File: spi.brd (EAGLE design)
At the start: 34 x 33 mm, 5 parts, among them IC2 25AA080SN, IC3 25AA080P, X1 2510-

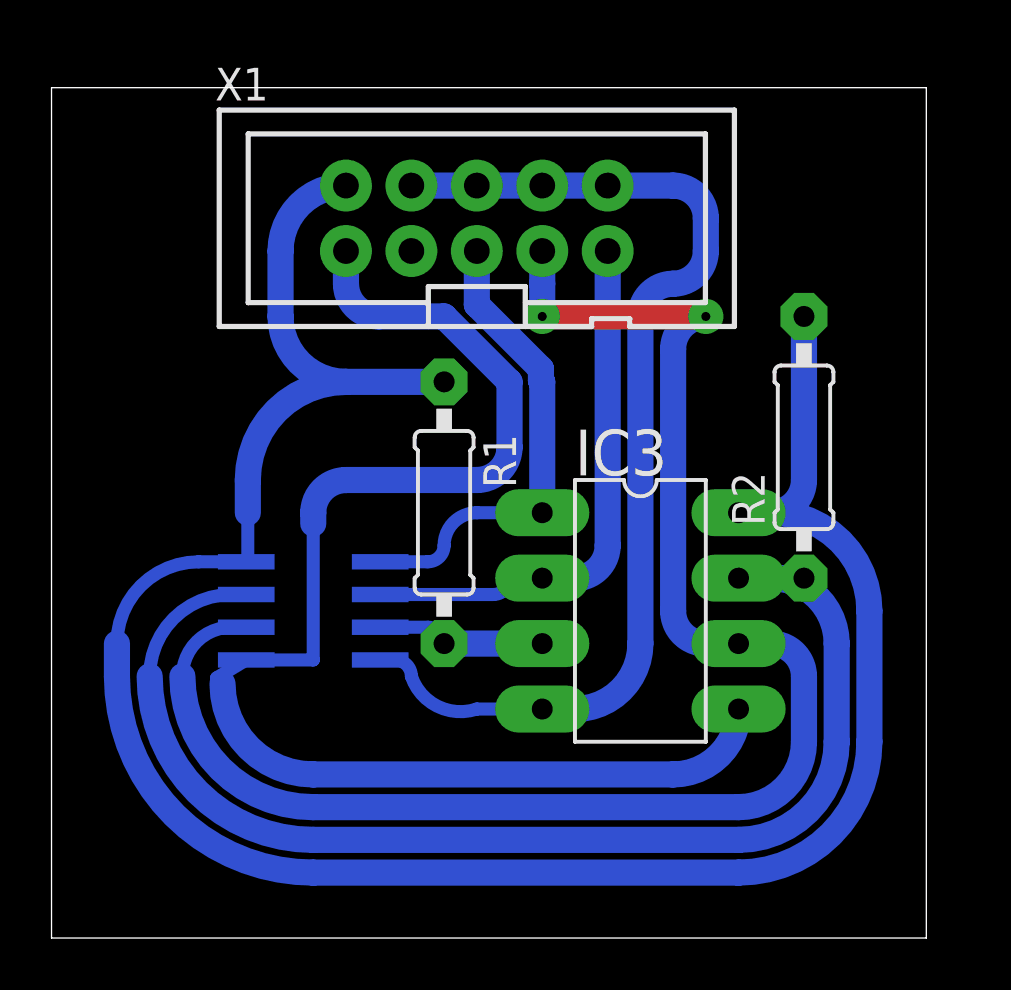
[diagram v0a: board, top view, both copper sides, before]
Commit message: Added ground polygon
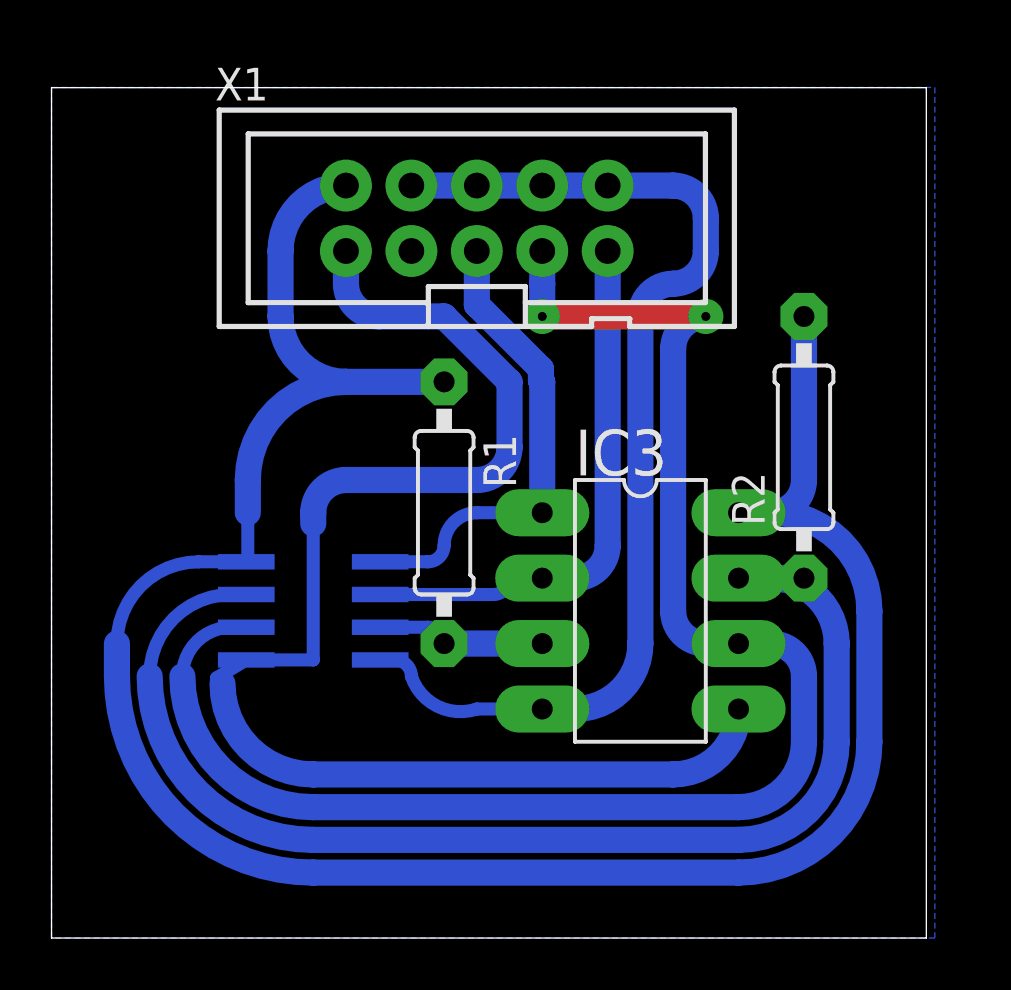
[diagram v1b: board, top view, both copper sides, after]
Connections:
- net N$1 renamed GND
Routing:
- added copper zone on layer 16, net GND
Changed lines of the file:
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@@
 <grid distance="50" unitdist="mil" unit="mm" style="lines" multiple="1" display="yes" altdistance="5" altunitdist="mil" altunit="mm"/>
 <layers>
-<layer number="1" name="Top" color="4" fill="1" visible="yes" active="yes"/>
+<layer number="1" name="Top" color="4" fill="1" visible="no" active="yes"/>
 <layer number="16" name="Bottom" color="1" fill="1" visible="yes" active="yes"/>
 <layer number="17" name="Pads" color="2" fill="1" visible="yes" active="yes"/>
 <layer number="18" name="Vias" color="2" fill="1" visible="yes" active="yes"/>
-<layer number="19" name="Unrouted" color="6" fill="1" visible="yes" active="yes"/>
+<layer number="19" name="Unrouted" color="6" fill="1" visible="no" active="yes"/>
 <layer number="20" name="Dimension" color="24" fill="1" visible="yes" active="yes"/>
-<layer number="21" name="tPlace" color="7" fill="1" visible="yes" active="yes"/>
-<layer number="22" name="bPlace" color="7" fill="1" visible="yes" active="yes"/>
-<layer number="23" name="tOrigins" color="15" fill="1" visible="yes" active="yes"/>
-<layer number="24" name="bOrigins" color="15" fill="1" visible="yes" active="yes"/>
-<layer number="25" name="tNames" color="7" fill="1" visible="yes" active="yes"/>
-<layer number="26" name="bNames" color="7" fill="1" visible="yes" active="yes"/>
-<layer number="27" name="tValues" color="7" fill="1" visible="yes" active="yes"/>
-<layer number="28" name="bValues" color="7" fill="1" visible="yes" active="yes"/>
-<layer number="29" name="tStop" color="7" fill="3" visible="yes" active="yes"/>
-<layer number="30" name="bStop" color="7" fill="6" visible="yes" active="yes"/>
-<layer number="31" name="tCream" color="7" fill="4" visible="yes" active="yes"/>
-<layer number="32" name="bCream" color="7" fill="5" visible="yes" active="yes"/>
-<layer number="33" name="tFinish" color="6" fill="3" visible="yes" active="yes"/>
-<layer number="34" name="bFinish" color="6" fill="6" visible="yes" active="yes"/>
-<layer number="35" name="tGlue" color="7" fill="4" visible="yes" active="yes"/>
-<layer number="36" name="bGlue" color="7" fill="5" visible="yes" active="yes"/>
-<layer number="37" name="tTest" color="7" fill="1" visible="yes" active="yes"/>
-<layer number="38" name="bTest" color="7" fill="1" visible="yes" active="yes"/>
-<layer number="39" name="tKeepout" color="4" fill="11" visible="yes" active="yes"/>
-<layer number="40" name="bKeepout" color="1" fill="11" visible="yes" active="yes"/>
-<layer number="41" name="tRestrict" color="4" fill="10" visible="yes" active="yes"/>
+<layer number="21" name="tPlace" color="7" fill="1" visible="no" active="yes"/>
+<layer number="22" name="bPlace" color="7" fill="1" visible="no" active="yes"/>
+<layer number="23" name="tOrigins" color="15" fill="1" visible="no" active="yes"/>
+<layer number="24" name="bOrigins" color="15" fill="1" visible="no" active="yes"/>
+<layer number="25" name="tNames" color="7" fill="1" visible="no" active="yes"/>
+<layer number="26" name="bNames" color="7" fill="1" visible="no" active="yes"/>
+<layer number="27" name="tValues" color="7" fill="1" visible="no" active="yes"/>
+<layer number="28" name="bValues" color="7" fill="1" visible="no" active="yes"/>
+<layer number="29" name="tStop" color="7" fill="3" visible="no" active="yes"/>
+<layer number="30" name="bStop" color="7" fill="6" visible="no" active="yes"/>
+<layer number="31" name="tCream" color="7" fill="4" visible="no" active="yes"/>
+<layer number="32" name="bCream" color="7" fill="5" visible="no" active="yes"/>
+<layer number="33" name="tFinish" color="6" fill="3" visible="no" active="yes"/>
+<layer number="34" name="bFinish" color="6" fill="6" visible="no" active="yes"/>
+<layer number="35" name="tGlue" color="7" fill="4" visible="no" active="yes"/>
+<layer number="36" name="bGlue" color="7" fill="5" visible="no" active="yes"/>
+<layer number="37" name="tTest" color="7" fill="1" visible="no" active="yes"/>
+<layer number="38" name="bTest" color="7" fill="1" visible="no" active="yes"/>
+<layer number="39" name="tKeepout" color="4" fill="11" visible="no" active="yes"/>
+<layer number="40" name="bKeepout" color="1" fill="11" visible="no" active="yes"/>
+<layer number="41" name="tRestrict" color="4" fill="10" visible="no" active="yes"/>
 <layer number="42" name="bRestrict" color="1" fill="10" visible="yes" active="yes"/>
-<layer number="43" name="vRestrict" color="2" fill="10" visible="yes" active="yes"/>
-<layer number="44" name="Drills" color="7" fill="1" visible="yes" active="yes"/>
-<layer number="45" name="Holes" color="7" fill="1" visible="yes" active="yes"/>
-<layer number="46" name="Milling" color="3" fill="1" visible="yes" active="yes"/>
-<layer number="47" name="Measures" color="7" fill="1" visible="yes" active="yes"/>
-<layer number="48" name="Document" color="7" fill="1" visible="yes" active="yes"/>
-<layer number="49" name="Reference" color="7" fill="1" visible="yes" active="yes"/>
-<layer number="51" name="tDocu" color="7" fill="1" visible="yes" active="yes"/>
-<layer number="52" name="bDocu" color="7" fill="1" visible="yes" active="yes"/>
+<layer number="43" name="vRestrict" color="2" fill="10" visible="no" active="yes"/>
+<layer number="44" name="Drills" color="7" fill="1" visible="no" active="yes"/>
+<layer number="45" name="Holes" color="7" fill="1" visible="no" active="yes"/>
+<layer number="46" name="Milling" color="3" fill="1" visible="no" active="yes"/>
+<layer number="47" name="Measures" color="7" fill="1" visible="no" active="yes"/>
+<layer number="48" name="Document" color="7" fill="1" visible="no" active="yes"/>
+<layer number="49" name="Reference" color="7" fill="1" visible="no" active="yes"/>
+<layer number="51" name="tDocu" color="7" fill="1" visible="no" active="yes"/>
+<layer number="52" name="bDocu" color="7" fill="1" visible="no" active="yes"/>
 <layer number="88" name="SimResults" color="9" fill="1" visible="no" active="no"/>
 <layer number="89" name="SimProbes" color="9" fill="1" visible="no" active="no"/>
@@
 <wire x1="42.85" y1="49.52" x2="8.89" y2="49.52" width="0" layer="20"/>
 <wire x1="8.89" y1="49.52" x2="8.89" y2="16.51" width="0" layer="20"/>
+<polygon width="0.3048" layer="42">
+<vertex x="19.05" y="27.94"/>
+<vertex x="19.05" y="34.29"/>
+<vertex x="25.4" y="34.29"/>
+<vertex x="25.4" y="27.94"/>
+</polygon>
 </plain>
 <attributes>
@@
 </elements>
 <signals>
-<signal name="N$1">
-<contactref element="IC2" pad="4"/>
-<contactref element="IC3" pad="4"/>
-<contactref element="X1" pad="4"/>
-<contactref element="X1" pad="6"/>
-<contactref element="X1" pad="8"/>
-<contactref element="X1" pad="10"/>
-<wire x1="21.65" y1="27.305" x2="22.225" y2="27.305" width="0.508" layer="16"/>
-<wire x1="22.225" y1="27.305" x2="22.86" y2="26.67" width="0.508" layer="16" curve="-90"/>
-<wire x1="22.86" y1="26.67" x2="25.4" y2="25.4" width="0.508" layer="16" curve="90"/>
-<wire x1="25.4" y1="25.4" x2="27.94" y2="25.4" width="0.508" layer="16"/>
-<wire x1="27.94" y1="25.4" x2="29.21" y2="25.4" width="1.016" layer="16"/>
-<wire x1="29.21" y1="25.4" x2="31.75" y2="27.94" width="1.016" layer="16" curve="90"/>
-<wire x1="31.75" y1="27.94" x2="31.75" y2="40.64" width="1.016" layer="16"/>
-<wire x1="31.75" y1="40.64" x2="33.02" y2="41.91" width="1.016" layer="16" curve="-90"/>
-<wire x1="33.02" y1="41.91" x2="34.29" y2="43.18" width="1.016" layer="16" curve="90"/>
-<wire x1="34.29" y1="43.18" x2="34.29" y2="44.45" width="1.016" layer="16"/>
-<wire x1="34.29" y1="44.45" x2="33.02" y2="45.72" width="1.016" layer="16" curve="90"/>
-<wire x1="33.02" y1="45.72" x2="30.48" y2="45.72" width="1.016" layer="16"/>
-<wire x1="22.86" y1="45.72" x2="25.4" y2="45.72" width="1.016" layer="16"/>
-<wire x1="25.4" y1="45.72" x2="27.94" y2="45.72" width="1.016" layer="16"/>
-<wire x1="27.94" y1="45.72" x2="30.48" y2="45.72" width="1.016" layer="16"/>
-</signal>
 <signal name="N$2">
 <contactref element="IC2" pad="8"/>
@@
 <wire x1="27.94" y1="27.94" x2="24.13" y2="27.94" width="1.016" layer="16"/>
 </signal>
+<signal name="GND">
+<contactref element="IC2" pad="4"/>
+<contactref element="IC3" pad="4"/>
+<contactref element="X1" pad="4"/>
+<contactref element="X1" pad="6"/>
+<contactref element="X1" pad="8"/>
+<contactref element="X1" pad="10"/>
+<wire x1="21.65" y1="27.305" x2="22.225" y2="27.305" width="0.508" layer="16"/>
+<wire x1="22.225" y1="27.305" x2="22.86" y2="26.67" width="0.508" layer="16" curve="-90"/>
+<wire x1="22.86" y1="26.67" x2="25.4" y2="25.4" width="0.508" layer="16" curve="90"/>
+<wire x1="25.4" y1="25.4" x2="27.94" y2="25.4" width="0.508" layer="16"/>
+<wire x1="27.94" y1="25.4" x2="29.21" y2="25.4" width="1.016" layer="16"/>
+<wire x1="29.21" y1="25.4" x2="31.75" y2="27.94" width="1.016" layer="16" curve="90"/>
+<wire x1="31.75" y1="27.94" x2="31.75" y2="40.64" width="1.016" layer="16"/>
+<wire x1="31.75" y1="40.64" x2="33.02" y2="41.91" width="1.016" layer="16" curve="-90"/>
+<wire x1="33.02" y1="41.91" x2="34.29" y2="43.18" width="1.016" layer="16" curve="90"/>
+<wire x1="34.29" y1="43.18" x2="34.29" y2="44.45" width="1.016" layer="16"/>
+<wire x1="34.29" y1="44.45" x2="33.02" y2="45.72" width="1.016" layer="16" curve="90"/>
+<wire x1="33.02" y1="45.72" x2="30.48" y2="45.72" width="1.016" layer="16"/>
+<wire x1="22.86" y1="45.72" x2="25.4" y2="45.72" width="1.016" layer="16"/>
+<wire x1="25.4" y1="45.72" x2="27.94" y2="45.72" width="1.016" layer="16"/>
+<wire x1="27.94" y1="45.72" x2="30.48" y2="45.72" width="1.016" layer="16"/>
+<polygon width="0.3048" layer="16" isolate="0.3048">
+<vertex x="8.89" y="49.53"/>
+<vertex x="43.18" y="49.53"/>
+<vertex x="43.18" y="16.51"/>
+<vertex x="8.89" y="16.51"/>
+</polygon>
+</signal>
 </signals>

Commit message: Renamed net
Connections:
- net N$2 renamed VCC
- net N$3 renamed SO
- net N$4 renamed HOLD
- net N$5 renamed SCK
- net N$6 renamed SI
- net N$7 renamed CS
- net N$8 renamed WP
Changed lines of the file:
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@@
 </elements>
 <signals>
-<signal name="N$2">
+<signal name="VCC">
 <contactref element="IC2" pad="8"/>
 <contactref element="IC3" pad="8"/>
@@
 <wire x1="16.51" y1="34.29" x2="16.51" y2="33.02" width="1.016" layer="16"/>
 </signal>
-<signal name="N$3">
+<signal name="SO">
 <contactref element="IC2" pad="2"/>
 <contactref element="IC3" pad="2"/>
@@
 <wire x1="30.48" y1="31.75" x2="30.48" y2="43.18" width="1.016" layer="16"/>
 </signal>
-<signal name="N$4">
+<signal name="HOLD">
 <contactref element="IC2" pad="7"/>
 <contactref element="IC3" pad="7"/>
@@
 <wire x1="35.56" y1="30.48" x2="38.1" y2="30.48" width="1.016" layer="16"/>
 </signal>
-<signal name="N$5">
+<signal name="SCK">
 <contactref element="IC2" pad="6"/>
 <contactref element="IC3" pad="6"/>
@@
 <wire x1="27.94" y1="40.64" x2="27.94" y2="41.90991875" width="1.016" layer="16"/>
 </signal>
-<signal name="N$6">
+<signal name="SI">
 <contactref element="IC2" pad="5"/>
 <contactref element="IC3" pad="5"/>
@@
 <wire x1="24.13" y1="40.64" x2="26.67" y2="38.1" width="1.016" layer="16"/>
 </signal>
-<signal name="N$7">
+<signal name="CS">
 <contactref element="IC2" pad="1"/>
 <contactref element="IC3" pad="1"/>
@@
 <wire x1="25.4" y1="41.0942125" x2="25.4" y2="43.18" width="1.016" layer="16"/>
 </signal>
-<signal name="N$8">
+<signal name="WP">
 <contactref element="IC2" pad="3"/>
 <contactref element="R1" pad="2"/>

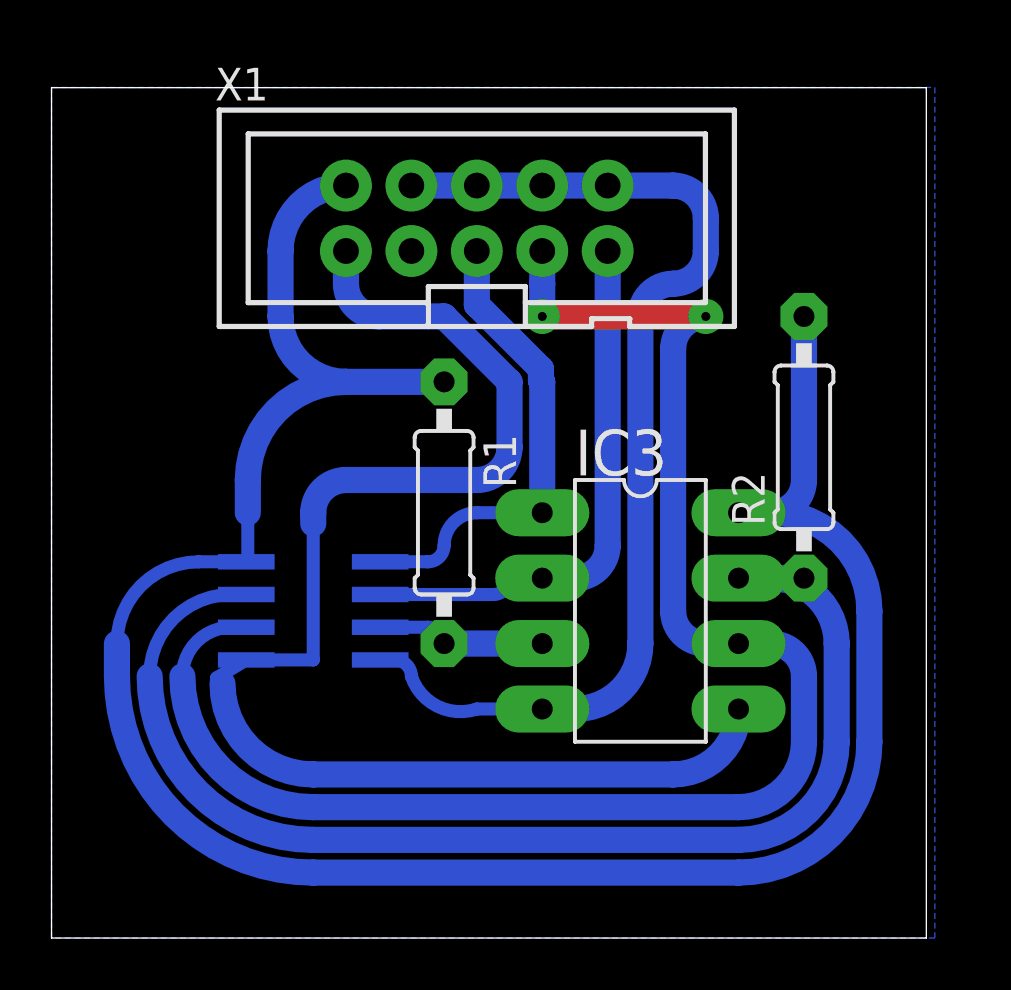
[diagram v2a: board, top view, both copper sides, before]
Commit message: Fixed DRC bugs
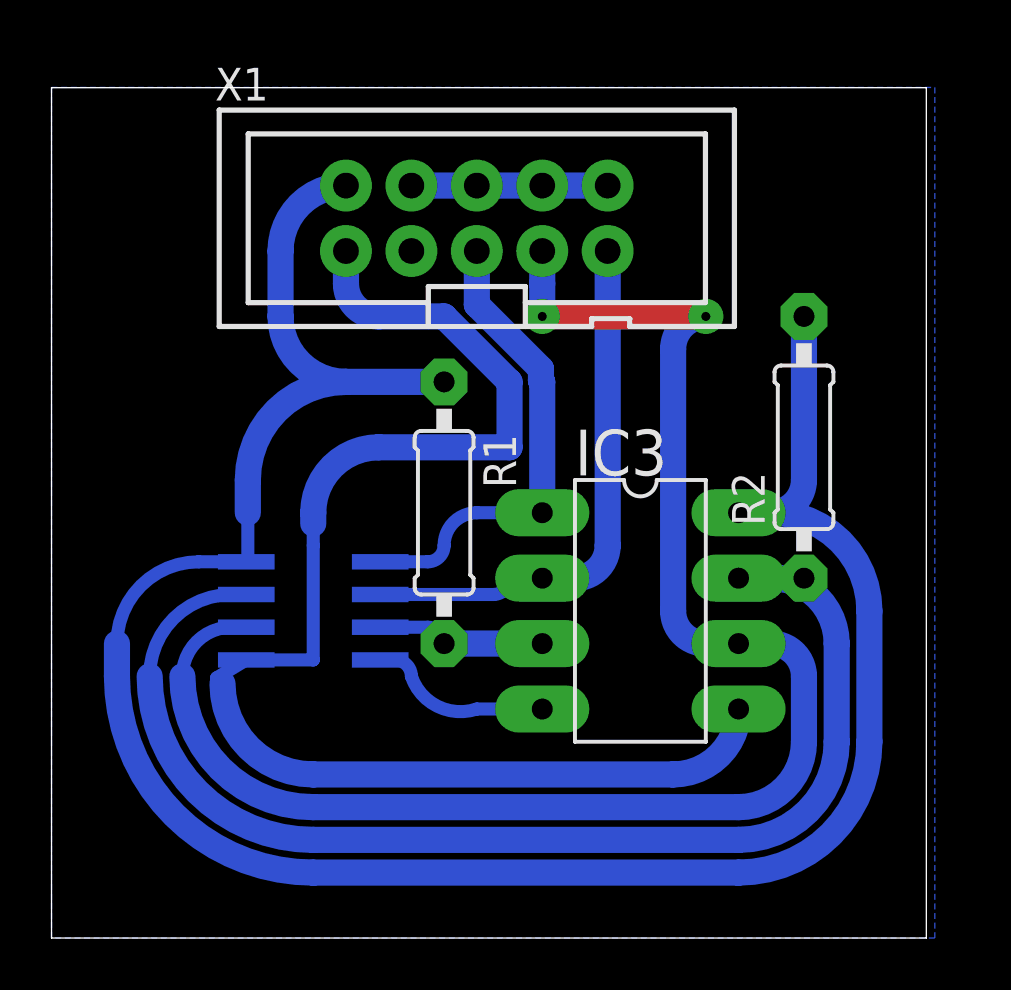
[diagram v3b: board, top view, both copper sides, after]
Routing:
- net GND: track 41.2 -> 14.5 mm
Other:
- board text added: "SPI25"
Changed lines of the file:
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@@
 <wire x1="8.89" y1="49.52" x2="8.89" y2="16.51" width="0" layer="20"/>
 <polygon width="0.3048" layer="42">
-<vertex x="19.05" y="27.94"/>
-<vertex x="19.05" y="34.29"/>
-<vertex x="25.4" y="34.29"/>
-<vertex x="25.4" y="27.94"/>
+<vertex x="20" y="27.94"/>
+<vertex x="20" y="31.75"/>
+<vertex x="20.32" y="31.75"/>
+<vertex x="20.32" y="27.94"/>
 </polygon>
+<text x="40.64" y="45.72" size="1.778" layer="42" rot="MR0">SPI25</text>
 </plain>
 <attributes>
@@
 <wire x1="15.5275" y1="26.3825" x2="15.3" y2="26.61" width="0.508" layer="16"/>
 <wire x1="16.45" y1="27.305" x2="19.05" y2="27.305" width="0.508" layer="16"/>
-<wire x1="19.05" y1="27.305" x2="19.05" y2="32.596665625" width="0.508" layer="16"/>
+<wire x1="19.05" y1="27.305" x2="19.05" y2="31.75" width="0.508" layer="16"/>
+<wire x1="19.05" y1="31.75" x2="19.05" y2="32.596665625" width="0.508" layer="16"/>
 <wire x1="16.45" y1="27.305" x2="15.3" y2="26.61" width="0.508" layer="16"/>
 <wire x1="20.32" y1="43.18" x2="20.32" y2="41.91" width="1.016" layer="16"/>
 <wire x1="21.59" y1="40.64" x2="20.32" y2="41.91" width="1.016" layer="16" curve="-90"/>
 <wire x1="19.05" y1="32.596665625" x2="19.05" y2="33.02" width="1.016" layer="16"/>
-<wire x1="19.05" y1="33.02" x2="20.32" y2="34.29" width="1.016" layer="16" curve="-90"/>
-<wire x1="20.32" y1="34.29" x2="25.4" y2="34.29" width="1.016" layer="16"/>
-<wire x1="25.4" y1="34.29" x2="26.67" y2="35.56" width="1.016" layer="16" curve="90"/>
+<wire x1="19.05" y1="33.02" x2="21.59" y2="35.56" width="1.016" layer="16" curve="-90"/>
+<wire x1="21.59" y1="35.56" x2="26.67" y2="35.56" width="1.016" layer="16"/>
 <wire x1="26.67" y1="38.1" x2="26.67" y2="35.56" width="1.016" layer="16"/>
 <wire x1="21.59" y1="40.64" x2="24.13" y2="40.64" width="1.016" layer="16"/>
@@
 <wire x1="22.86" y1="26.67" x2="25.4" y2="25.4" width="0.508" layer="16" curve="90"/>
 <wire x1="25.4" y1="25.4" x2="27.94" y2="25.4" width="0.508" layer="16"/>
-<wire x1="27.94" y1="25.4" x2="29.21" y2="25.4" width="1.016" layer="16"/>
-<wire x1="29.21" y1="25.4" x2="31.75" y2="27.94" width="1.016" layer="16" curve="90"/>
-<wire x1="31.75" y1="27.94" x2="31.75" y2="40.64" width="1.016" layer="16"/>
-<wire x1="31.75" y1="40.64" x2="33.02" y2="41.91" width="1.016" layer="16" curve="-90"/>
-<wire x1="33.02" y1="41.91" x2="34.29" y2="43.18" width="1.016" layer="16" curve="90"/>
-<wire x1="34.29" y1="43.18" x2="34.29" y2="44.45" width="1.016" layer="16"/>
-<wire x1="34.29" y1="44.45" x2="33.02" y2="45.72" width="1.016" layer="16" curve="90"/>
-<wire x1="33.02" y1="45.72" x2="30.48" y2="45.72" width="1.016" layer="16"/>
 <wire x1="22.86" y1="45.72" x2="25.4" y2="45.72" width="1.016" layer="16"/>
 <wire x1="25.4" y1="45.72" x2="27.94" y2="45.72" width="1.016" layer="16"/>
